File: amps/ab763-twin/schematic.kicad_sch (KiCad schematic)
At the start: 130 parts, among them T1 125P34A · 340-0-340 V, T2 125C1A, T3 125A29A, T4 125A20B

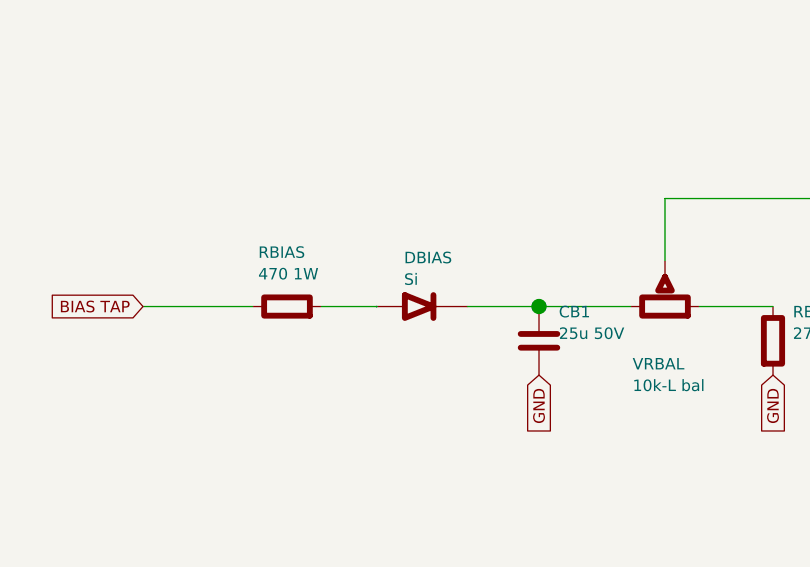
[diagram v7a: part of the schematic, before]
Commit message: Fix: 17 bias rectifiers and six HT diodes drawn backwards; the 6G6-B and 6G4 bias rows as their drawings show; AA1164 V4 units
Rectifier polarity has no gate. The netlists model every supply as an ideal
source, the sheet-vs-board check treats a two-terminal part as unordered, and
the boards' `cathode:` fields were copied from the sheets. Measured over all
68 diodes on 40 sheets: 18 negative-bias rectifiers had the cathode on the
negative node (a diode that way round would charge the node POSITIVE), and all
six 6G6-B HT diodes pointed away from B+. The printed negative bias on each of
those sheets falsifies the drawn orientation; the nine bias rectifiers already
right (AA1164, AA864, AB165, B15N, DR103, JTM100, M1959, M2204, 6G6-B) show
the idiom. Flipped: 5E4-A, 5E5-A, 5E6-A, 5F10, 5F4, 5F6, 5F6-A, 5F8-A, 5G9,
6G2, 6G3, 6G4, 6G5, AA964, AB763, AB763 Super, AB763 Twin, JTM45 (the
M1987's is with the Marshall board repair) and the 6G6-B's DR1-DR6. The
5F8-A board, which had copied its sheet, has the band moved to the tap side;
the other boards' bands are with the board-repair wave. A gate is next.

6G6-B bias. E-FB (6431x3364): the 1K 1W rises from TR1's SECOND secondary
terminal, a bias tap between the upper HT end and the grounded centre tap,
to the diode's + end. The sheet fed the diode from the HT end with the 1K
after it. T1 now carries its tap pin and the row reads tap -> 1K -> diode ->
-54 V. (The triage had read "HT end"; the native crop shows the tap.)

6G4 bias. A-FJ, read natively: tap -> rectifier -> 8 uF -> 10K -> the -55 V
node, which carries a second 8 uF and the 56K to ground as a bleeder. The
sheet fed the rectifier from an HT end, drew the 56K in series and carried
one capacitor. CBIAS2 joins the parts list, and RBIAS1's role now says
bleeder.

AA1164 V4. The K-FD sheet prints the phase inverter 7/6/8 and the tremolo
oscillator 2/1/3 (5554x4346); the sheet had them the other way round.

Gates: check_schematics 40/0 (+selftest), verify_schematic_nets 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
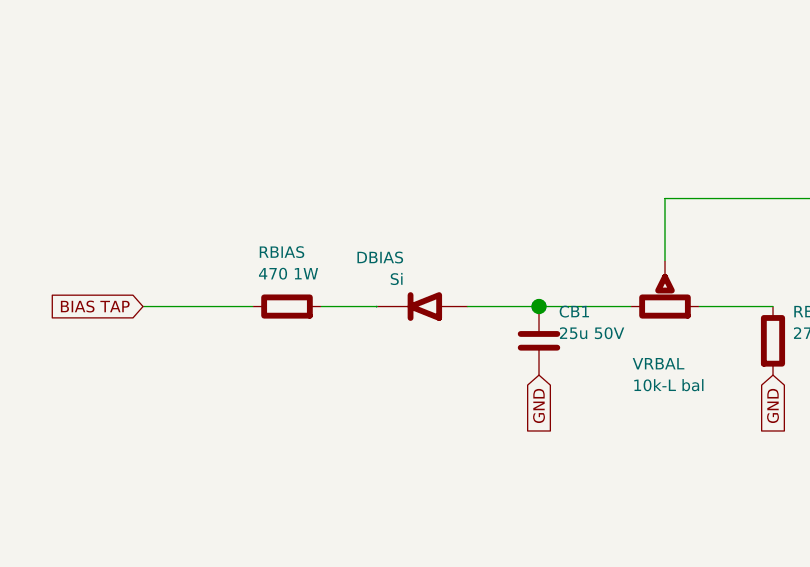
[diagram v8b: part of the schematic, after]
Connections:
- net at CB1.1, VRBAL.1: now also DBIAS.1 (A); no longer DBIAS.2 (K)
- net at RBIAS.2: now also DBIAS.2 (K); no longer DBIAS.1 (A)
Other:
- moved on the sheet: DBIAS
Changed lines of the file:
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@@
   (wire (pts (xy 469.529 325.889) (xy 469.609 325.889))
     (stroke (width 0) (type default)))
-  (symbol (lib_id "cx:DIODE_SS") (at 474.609 325.889 0) (unit 1)
+  (symbol (lib_id "cx:DIODE_SS") (at 474.609 325.889 180) (unit 1)
     (in_bom yes) (on_board yes)
     (property "Reference" "DBIAS" (at 472.609 320.489 0) (effects (font (size 1.27 1.27)) (justify left)))
